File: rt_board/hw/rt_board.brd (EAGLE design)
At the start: 63.8 x 73.7 mm, 72 parts, among them IC1 MCP170333MB, IC2/L1 TLE4935L, IC3/L2 TLE4935L, IC4/R1 TLE4935L, IC5/R2 TLE4935L, Q1 8MHz, SW1 B3U-1000PM-B, SW2 B3U-1000PM-B, U1 DRV8801PWP, U2 DRV8801PWP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

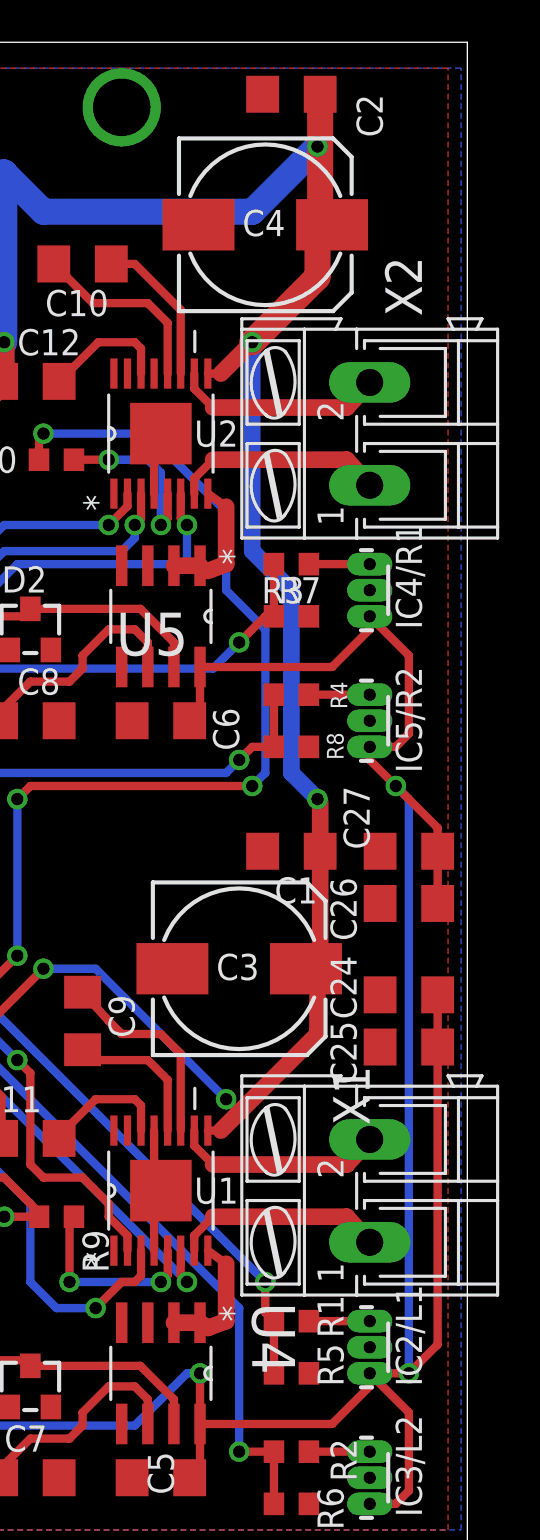
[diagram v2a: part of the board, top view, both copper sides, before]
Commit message: slight elements replacement, so that more space around power connectors will be available
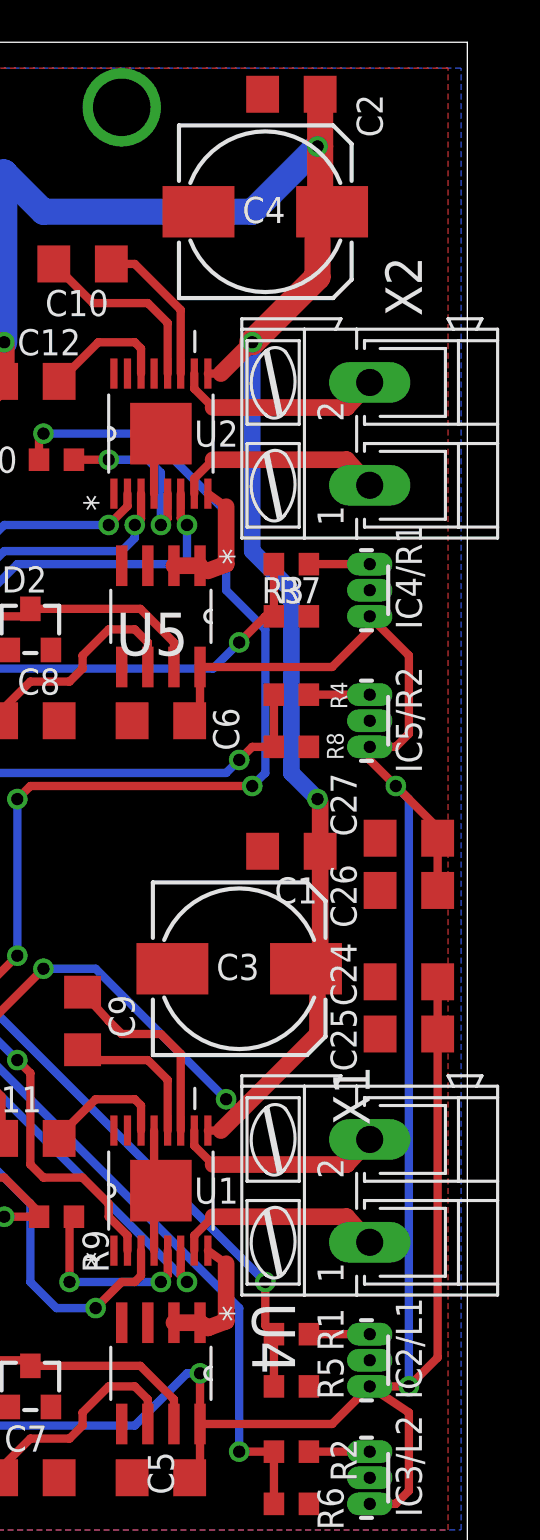
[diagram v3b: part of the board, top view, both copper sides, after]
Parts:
- moved C25 0.64 mm to (71.8, 31.8)
- moved IC2/L1 0.64 mm to (69.8, 15.9)
- moved R1 0.64 mm to (66.0, 17.1)
- moved R5 0.63 mm to (66.0, 14.6)
- moved C24 0.63 mm to (71.8, 34.3)
- moved C26 0.63 mm to (71.8, 38.7)
- moved C27 0.63 mm to (71.8, 41.3)
- moved C4 0.63 mm to (64.8, 71.8)
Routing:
- net N$17: track 39.5 -> 40.2 mm
- net +12V: track 120.4 -> 120.9 mm
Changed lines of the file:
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@@
 <attribute name="VALUE" x="23.495" y="25.0825" size="1.27" layer="27" rot="R180"/>
 </element>
-<element name="IC2/L1" library="allegro" package="SIP3-UA" value="TLE4935L" x="69.85" y="16.51" smashed="yes" rot="R90">
-<attribute name="OC_NEWARK" value="unknown" x="69.85" y="16.51" size="1.778" layer="27" rot="R90" display="off"/>
-<attribute name="MPN" value="" x="69.85" y="16.51" size="1.778" layer="27" rot="R90" display="off"/>
-<attribute name="MF" value="" x="69.85" y="16.51" size="1.778" layer="27" rot="R90" display="off"/>
-<attribute name="OC_FARNELL" value="unknown" x="69.85" y="16.51" size="1.778" layer="27" rot="R90" display="off"/>
-<attribute name="NAME" x="72.39" y="14.605" size="1.27" layer="25" rot="R90"/>
-<attribute name="VALUE" x="73.025" y="19.05" size="0.8128" layer="27" rot="R270"/>
-</element>
-<element name="R1" library="rcl" package="R0603" value="2kR" x="66.04" y="17.78" smashed="yes" rot="R180">
-<attribute name="NAME" x="67.31" y="19.05" size="1.27" layer="25" rot="R270"/>
-<attribute name="VALUE" x="68.58" y="20.32" size="1.27" layer="27" rot="R180"/>
-</element>
-<element name="R5" library="rcl" package="R0603" value="3kR" x="66.04" y="15.24" smashed="yes">
-<attribute name="NAME" x="68.58" y="14.605" size="1.27" layer="25" rot="R90"/>
-<attribute name="VALUE" x="63.5" y="13.335" size="1.27" layer="27"/>
+<element name="IC2/L1" library="allegro" package="SIP3-UA" value="TLE4935L" x="69.85" y="15.875" smashed="yes" rot="R90">
+<attribute name="OC_NEWARK" value="unknown" x="69.85" y="15.875" size="1.778" layer="27" rot="R90" display="off"/>
+<attribute name="MPN" value="" x="69.85" y="15.875" size="1.778" layer="27" rot="R90" display="off"/>
+<attribute name="MF" value="" x="69.85" y="15.875" size="1.778" layer="27" rot="R90" display="off"/>
+<attribute name="OC_FARNELL" value="unknown" x="69.85" y="15.875" size="1.778" layer="27" rot="R90" display="off"/>
+<attribute name="NAME" x="72.39" y="13.97" size="1.27" layer="25" rot="R90"/>
+<attribute name="VALUE" x="73.025" y="18.415" size="0.8128" layer="27" rot="R270"/>
+</element>
+<element name="R1" library="rcl" package="R0603" value="2kR" x="66.04" y="17.145" smashed="yes" rot="R180">
+<attribute name="NAME" x="67.31" y="18.415" size="1.27" layer="25" rot="R270"/>
+<attribute name="VALUE" x="68.58" y="19.685" size="1.27" layer="27" rot="R180"/>
+</element>
+<element name="R5" library="rcl" package="R0603" value="3kR" x="66.04" y="14.605" smashed="yes">
+<attribute name="NAME" x="68.58" y="13.97" size="1.27" layer="25" rot="R90"/>
+<attribute name="VALUE" x="63.5" y="12.7" size="1.27" layer="27"/>
 </element>
 <element name="IC3/L2" library="allegro" package="SIP3-UA" value="TLE4935L" x="69.85" y="10.16" smashed="yes" rot="R90">
@@
 <attribute name="VALUE" x="67.31" y="76.2" size="1.27" layer="27" rot="R180"/>
 </element>
-<element name="C4" library="rcl" package="153CLV-0810" value="100uF" x="64.77" y="71.12" smashed="yes">
-<attribute name="NAME" x="63.655" y="70.57" size="1.27" layer="25"/>
-<attribute name="VALUE" x="62.35" y="67.875" size="1.27" layer="27"/>
+<element name="C4" library="rcl" package="153CLV-0810" value="100uF" x="64.77" y="71.755" smashed="yes">
+<attribute name="NAME" x="63.655" y="71.205" size="1.27" layer="25"/>
+<attribute name="VALUE" x="62.35" y="68.51" size="1.27" layer="27"/>
 </element>
 <element name="U5" library="Allegro-ACS712ELCTR-20A-T" package="SOIC127P600X175-8N" value="ACS712ELCTR-05B-T" x="59.69" y="52.07" smashed="yes" rot="R270">
@@
 <attribute name="VALUE" x="41.03" y="64.97" size="1.27" layer="27"/>
 </element>
-<element name="C24" library="rcl" package="C1206" value="100nF" x="71.755" y="33.655" smashed="yes" rot="R180">
-<attribute name="NAME" x="67.945" y="35.56" size="1.27" layer="25" rot="R270"/>
+<element name="C24" library="rcl" package="C1206" value="100nF" x="71.755" y="34.29" smashed="yes" rot="R180">
+<attribute name="NAME" x="67.945" y="36.195" size="1.27" layer="25" rot="R270"/>
 <attribute name="VALUE" x="73.66" y="36.195" size="1.27" layer="27" rot="R180"/>
 </element>
-<element name="C25" library="rcl" package="C1206" value="100nF" x="71.755" y="31.115" smashed="yes" rot="R180">
-<attribute name="NAME" x="67.945" y="32.385" size="1.27" layer="25" rot="R270"/>
-<attribute name="VALUE" x="73.66" y="29.845" size="1.27" layer="27" rot="R180"/>
-</element>
-<element name="C26" library="rcl" package="C1206" value="100nF" x="71.755" y="38.1" smashed="yes" rot="R180">
-<attribute name="NAME" x="67.945" y="39.37" size="1.27" layer="25" rot="R270"/>
-<attribute name="VALUE" x="73.66" y="36.83" size="1.27" layer="27" rot="R180"/>
-</element>
-<element name="C27" library="rcl" package="C1206" value="100nF" x="71.755" y="40.64" smashed="yes" rot="R180">
-<attribute name="NAME" x="68.58" y="43.815" size="1.27" layer="25" rot="R270"/>
-<attribute name="VALUE" x="74.295" y="43.18" size="1.27" layer="27" rot="R180"/>
+<element name="C25" library="rcl" package="C1206" value="100nF" x="71.755" y="31.75" smashed="yes" rot="R180">
+<attribute name="NAME" x="67.945" y="33.02" size="1.27" layer="25" rot="R270"/>
+<attribute name="VALUE" x="73.66" y="30.48" size="1.27" layer="27" rot="R180"/>
+</element>
+<element name="C26" library="rcl" package="C1206" value="100nF" x="71.755" y="38.735" smashed="yes" rot="R180">
+<attribute name="NAME" x="67.945" y="40.005" size="1.27" layer="25" rot="R270"/>
+<attribute name="VALUE" x="73.66" y="37.465" size="1.27" layer="27" rot="R180"/>
+</element>
+<element name="C27" library="rcl" package="C1206" value="100nF" x="71.755" y="41.275" smashed="yes" rot="R180">
+<attribute name="NAME" x="67.945" y="44.45" size="1.27" layer="25" rot="R270"/>
+<attribute name="VALUE" x="74.295" y="43.815" size="1.27" layer="27" rot="R180"/>
 </element>
 </elements>
@@
 <wire x1="67.31" y1="68.58" x2="67.31" y2="70.41" width="1.27" layer="1"/>
 <wire x1="67.31" y1="70.41" x2="67.665" y2="70.765" width="0.4064" layer="1"/>
-<wire x1="67.665" y1="70.765" x2="68.02" y2="71.12" width="0.4064" layer="1"/>
+<wire x1="67.665" y1="70.765" x2="68.02" y2="71.755" width="0.4064" layer="1"/>
 <wire x1="67.44" y1="77.47" x2="67.44" y2="74.93" width="1.27" layer="1"/>
 <wire x1="67.44" y1="74.93" x2="67.44" y2="70.99" width="1.27" layer="1"/>
@@
 <wire x1="61.595" y1="12.7762" x2="68.0212" y2="12.7762" width="0.4064" layer="1"/>
 <wire x1="68.0212" y1="12.7762" x2="69.85" y2="14.605" width="0.4064" layer="1"/>
-<wire x1="69.85" y1="14.605" x2="69.85" y2="15.24" width="0.4064" layer="1"/>
 <wire x1="69.85" y1="8.89" x2="71.12" y2="8.89" width="0.4064" layer="1"/>
 <wire x1="71.12" y1="8.89" x2="71.755" y2="9.525" width="0.4064" layer="1"/>
 <wire x1="71.755" y1="9.525" x2="71.755" y2="13.335" width="0.4064" layer="1"/>
-<wire x1="71.755" y1="13.335" x2="69.85" y2="15.24" width="0.4064" layer="1"/>
+<wire x1="71.755" y1="13.335" x2="69.85" y2="14.605" width="0.4064" layer="1"/>
 <wire x1="61.595" y1="49.6062" x2="61.595" y2="47.495" width="0.4064" layer="1"/>
 <wire x1="61.595" y1="47.495" x2="61.09" y2="46.99" width="0.4064" layer="1"/>
@@
 <wire x1="71.755" y1="46.355" x2="71.755" y2="50.165" width="0.4064" layer="1"/>
 <wire x1="71.755" y1="50.165" x2="69.85" y2="52.07" width="0.4064" layer="1"/>
-<wire x1="69.85" y1="15.24" x2="71.755" y2="15.24" width="0.4064" layer="1"/>
-<via x="71.755" y="15.24" extent="1-16" drill="0.6"/>
-<wire x1="71.755" y1="15.24" x2="71.755" y2="43.18" width="0.4064" layer="16"/>
+<wire x1="69.85" y1="14.605" x2="71.755" y2="14.605" width="0.4064" layer="1"/>
+<via x="71.755" y="14.605" extent="1-16" drill="0.6"/>
+<wire x1="71.755" y1="14.605" x2="71.755" y2="43.18" width="0.4064" layer="16"/>
 <wire x1="71.755" y1="43.18" x2="71.12" y2="43.815" width="0.4064" layer="16"/>
 <via x="71.12" y="43.815" extent="1-16" drill="0.6"/>
@@
 <contactref element="C24" pad="1"/>
 <contactref element="C25" pad="1"/>
-<wire x1="73.155" y1="40.64" x2="73.155" y2="38.1" width="0.4064" layer="1"/>
-<wire x1="73.155" y1="40.64" x2="73.155" y2="41.78" width="0.4064" layer="1"/>
+<wire x1="73.155" y1="41.275" x2="73.155" y2="38.735" width="0.4064" layer="1"/>
+<wire x1="73.155" y1="41.275" x2="73.155" y2="41.78" width="0.4064" layer="1"/>
 <wire x1="73.155" y1="41.78" x2="71.12" y2="43.815" width="0.4064" layer="1"/>
-<wire x1="73.155" y1="31.115" x2="73.155" y2="16.64" width="0.4064" layer="1"/>
-<wire x1="73.155" y1="16.64" x2="71.755" y2="15.24" width="0.4064" layer="1"/>
-<wire x1="73.155" y1="33.655" x2="73.155" y2="31.115" width="0.4064" layer="1"/>
+<wire x1="73.155" y1="31.75" x2="73.155" y2="16.005" width="0.4064" layer="1"/>
+<wire x1="73.155" y1="16.005" x2="71.755" y2="14.605" width="0.4064" layer="1"/>
+<wire x1="73.155" y1="34.29" x2="73.155" y2="31.75" width="0.4064" layer="1"/>
 </signal>
 <signal name="N$11">
@@
 <contactref element="IC2/L1" pad="3"/>
 <contactref element="R1" pad="1"/>
-<wire x1="69.85" y1="17.78" x2="66.89" y2="17.78" width="0.4064" layer="1"/>
+<wire x1="69.85" y1="17.145" x2="66.89" y2="17.145" width="0.4064" layer="1"/>
 </signal>
 <signal name="N$17">
@@
 <contactref element="R5" pad="1"/>
 <contactref element="U6" pad="41"/>
-<wire x1="65.19" y1="17.78" x2="65.19" y2="15.24" width="0.4064" layer="1"/>
+<wire x1="65.19" y1="17.145" x2="65.19" y2="14.605" width="0.4064" layer="1"/>
 <wire x1="38.6334" y1="40.894" x2="39.751" y2="40.894" width="0.4064" layer="1"/>
 <wire x1="39.751" y1="40.894" x2="42.545" y2="38.1" width="0.4064" layer="1"/>
@@
 <wire x1="46.355" y1="38.1" x2="64.77" y2="19.685" width="0.4064" layer="16"/>
 <via x="64.77" y="19.685" extent="1-16" drill="0.6"/>
-<wire x1="64.77" y1="19.685" x2="64.77" y2="18.2" width="0.4064" layer="1"/>
-<wire x1="64.77" y1="18.2" x2="65.19" y2="17.78" width="0.4064" layer="1"/>
+<wire x1="64.77" y1="19.685" x2="64.77" y2="17.565" width="0.4064" layer="1"/>
+<wire x1="64.77" y1="17.565" x2="65.19" y2="17.145" width="0.4064" layer="1"/>
 </signal>
 <signal name="N$18">
